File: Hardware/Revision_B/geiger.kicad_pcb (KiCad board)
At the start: 2 copper layers, 123.1 x 31.9 mm, 30 parts, among them J1 I2C 5V, J2 I2C 3V3, J3 GND, U1 BSP125

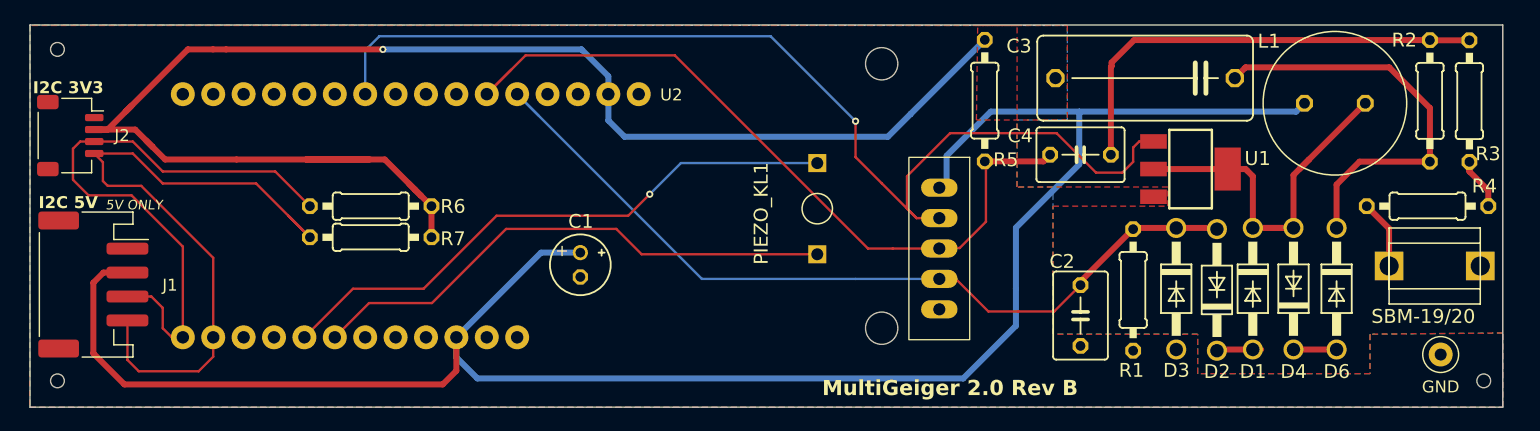
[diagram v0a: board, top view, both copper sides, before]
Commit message: Hardware: Rev B V2 + Rev C V2 — layout update to remove HV-to-counter crosstalk
Why these boards were redesigned:

The previous Rev B (Feather form factor) and Rev C (XIAO form factor)
carrier PCBs could register phantom Geiger counts: each pulse of the
high-voltage boost supply coupled a small spike into the tube counting
input. Long-term field data and bench probing traced the root cause to
the layout, not the circuit:

- The module socket pinout placed the counting input (GMZ_COUNT) directly
  beside the HV regulation sense net (HV_CAP_FUL), 2.54 mm pad to pad, so
  the most sensitive high-impedance node on the board (1 Mohm) was forced
  to run alongside its noisiest neighbour before routing even started.
- The counting trace crossed gaps in the ground plane (the worst void sat
  under the unused JP1 header on Rev B), weakening its return path exactly
  where the coupling occurred.

Firmware (V2.6.31+) fully compensates the phantom pulses by blanking, so
deployed nodes read correctly, but these V2 boards remove the coupling at
the source. What changed vs the previous revisions:

- Pin roles swapped at the module socket: GMZ_COUNT <-> HV_FET_OUT. The
  counting input now sits >=10 mm from both HV nets; the FET gate (a
  driven, low-impedance net) takes the seat next to the HV sense line.
- JP1 removed (Rev B), closing the ground-plane slot its through-holes cut.
- Routing rules enforced by DRC: >=2 mm clearance between the counting
  trace and both HV nets; crossings only on the opposite layer at 90 deg.
- Ground rebuilt: solid pours both sides with ~700 stitching vias; ground
  return coverage under the counting trace raised from ~79% to ~87%
  (Rev B; Rev C similar). The previous boards had no stitching vias near
  the counting run.
- Mounting holes enlarged 2.2 -> 2.7 mm to suit M2.5 hardware.
- The HV generation circuit itself is deliberately untouched: same
  schematic, same BOM, same tube chain.

IMPORTANT — FIRMWARE COMPATIBILITY: the pin-role swap makes b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
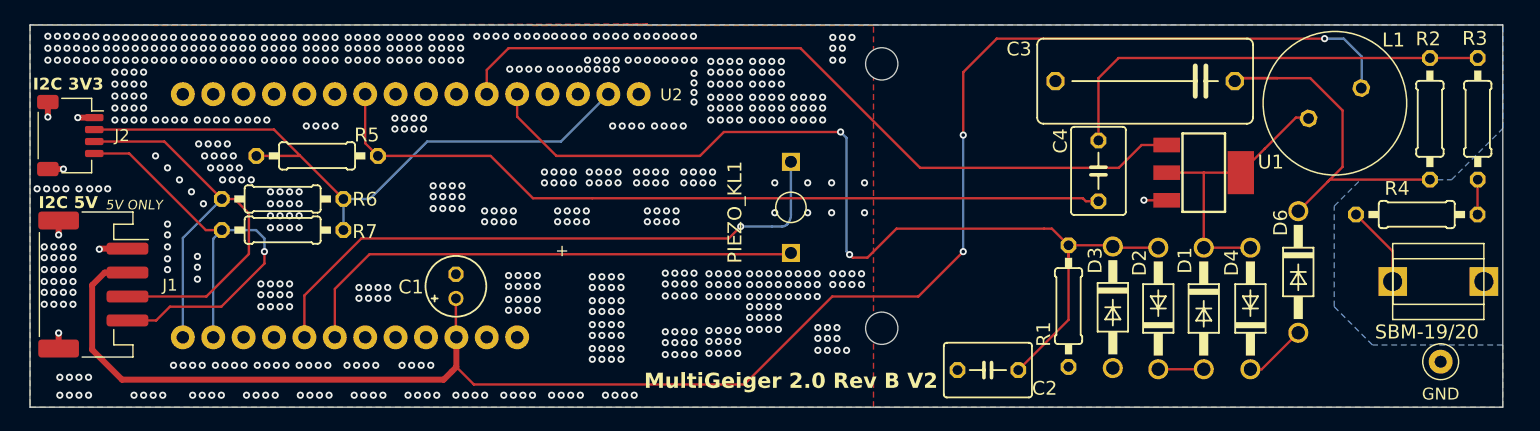
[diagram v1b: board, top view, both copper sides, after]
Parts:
- removed JP1: , geiger:1X05_325
- removed the REF** at (103.2, 124.1)
- removed the REF** at (172.1, 147.4)
- removed the REF** at (172.1, 125.3)
- removed the REF** at (103.2, 151.8)
- removed the REF** at (222.4, 151.8)
- added REF**: MountingHole_2.7mm_M2.5, MountingHole:MountingHole_2.7mm_M2.5, F.Cu at (172.1, 125.4)
- added REF**: MountingHole_2.7mm_M2.5, MountingHole:MountingHole_2.7mm_M2.5, F.Cu at (172.1, 147.5)
- R3, R4: value 2M7 -> 4M7
- moved R5 56.0 mm to (124.9, 133.0), turned to 0 degrees
- moved C1 10.6 mm to (136.5, 143.9), turned to 90 degrees
- moved C2 8.98 mm to (181.0, 150.9), turned to 180 degrees
- moved R6 7.38 mm to (122.0, 136.6)
- moved R7 7.38 mm to (122.0, 139.2)
- moved R1 5.57 mm to (187.7, 145.6)
- moved D3 5.52 mm to (191.4, 145.7)
- moved D2 5.14 mm to (195.2, 145.8)
- moved D1 4.42 mm to (199.0, 145.8)
- moved D4 3.96 mm to (202.9, 145.8)
- moved D6 3.49 mm to (206.9, 142.7)
- moved PIEZO_KL1 2.20 mm to (164.5, 137.3)
- moved C4 2.02 mm to (190.2, 134.3), turned to -90 degrees
- moved R3 1.64 mm to (221.9, 129.9)
- moved R2 1.50 mm to (217.9, 129.9)
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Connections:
- U2 pad 19: /HV_FET_OUT -> /GMZ_COUNT
- U2 pad 23: /GMZ_COUNT -> /HV_FET_OUT
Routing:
- net +3V3: track 127.4 -> 55.2 mm, vias 1 -> 0
- net /HV_FET_OUT: track 89.3 -> 64.5 mm, vias 1 -> 0
- net +5V: track 162.8 -> 146.7 mm, vias 0 -> 3
- net /SCL: track 57.6 -> 41.9 mm, vias 0 -> 1
- net /HV_CAP_FUL: track 71.2 -> 83.4 mm, vias 0 -> 2
- net GND: track 0.00 -> 10.7 mm, vias 0 -> 698
- net Net-(D1-K): track 33.5 -> 24.0 mm
- net /SDA: track 51.4 -> 43.3 mm
- net /GMZ_COUNT: track 63.5 -> 67.6 mm
- net /SPEAKER_N: track 48.9 -> 51.6 mm
- net Net-(C3-Pad1): track 34.8 -> 32.3 mm
- net Net-(D4-K): track 3.10 -> 5.26 mm
- net /SPEAKER_P: track 45.0 -> 43.4 mm
- net Net-(R3-Pad2): track 4.35 -> 2.93 mm
- net Net-(SBM-19/20-1): track 5.77 -> 6.87 mm
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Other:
- board text added: "MultiGeiger 2.0 Rev B V2"
- board text removed: "MultiGeiger 2.0 Rev B"

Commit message: Hardware Rev B V2: remove stray "+" from silkscreen, add order-ready Gerber zips
The front silk carried a lone "+" text at (144.8, 141.5), a leftover
from the earlier Rev B layout. On this board it sits under the module
socket and labels nothing, so it is removed from the board source and
the exported Deliverables Gerber (geiger-F_Silkscreen.gbr).

Silkscreen-only change: the re-exported Gerber diff shows only the two
"+" strokes disappearing; copper, mask, paste, drill, and edge layers
are unchanged. DRC clean (0 violations).

Also adds Deliverables/Gerber Files.zip for both Rev B V2 and Rev C V2
- the complete fabrication upload packages (all Gerber + drill files)
so the boards can be re-ordered directly from the repository.
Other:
- board text removed: "+"
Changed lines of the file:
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@@
-		)
-	)
-	(gr_text "+"
-		(at 144.816196 141.54757 0)
-		(layer "F.SilkS")
-		(effects
-			(font
-				(size 1 1)
-				(thickness 0.15)
-			)
-			(justify left bottom)
 		)
 	)
